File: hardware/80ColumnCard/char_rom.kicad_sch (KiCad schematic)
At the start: 3 parts, among them U20 2732, U20W28 '64 - '512, U20W32 '010 - '080

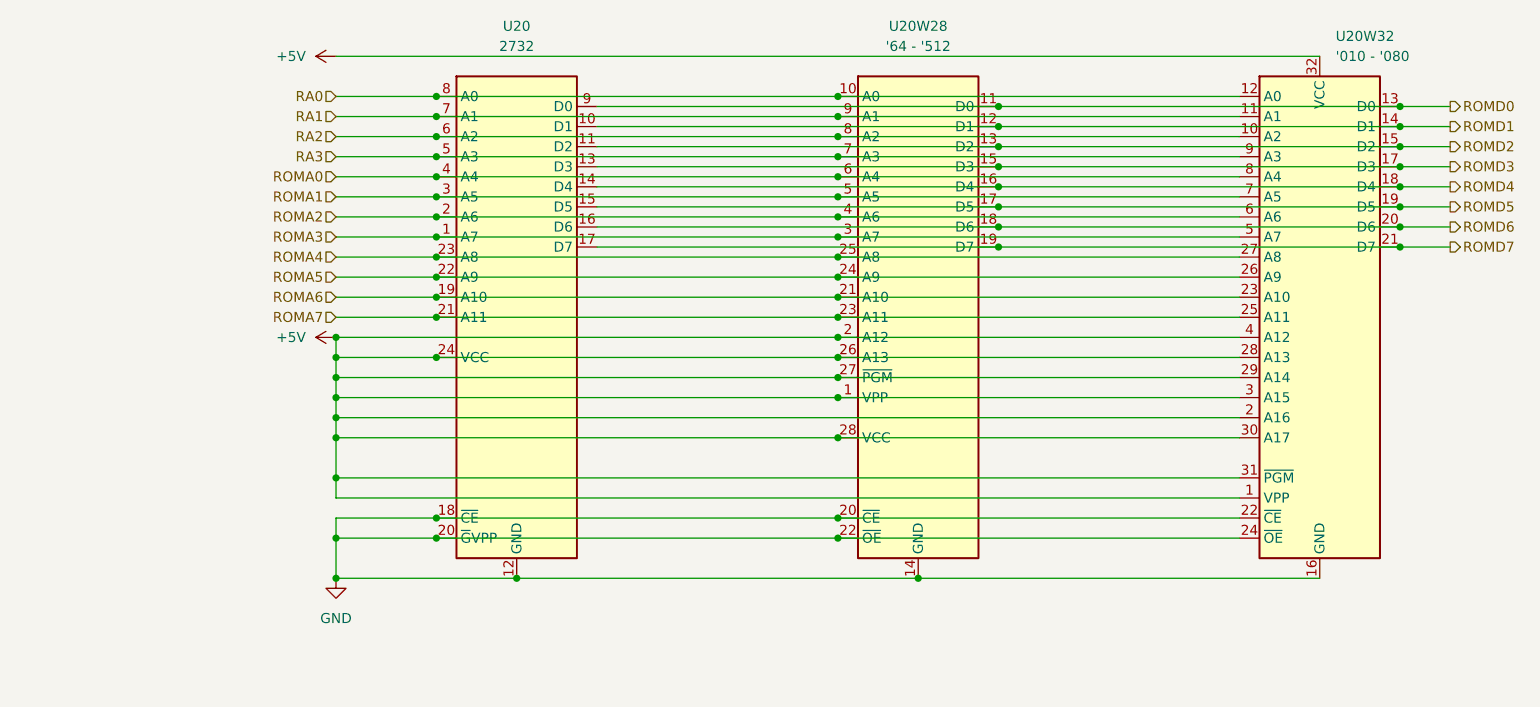
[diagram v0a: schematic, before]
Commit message: clean up, add jumpers for fw/char selection
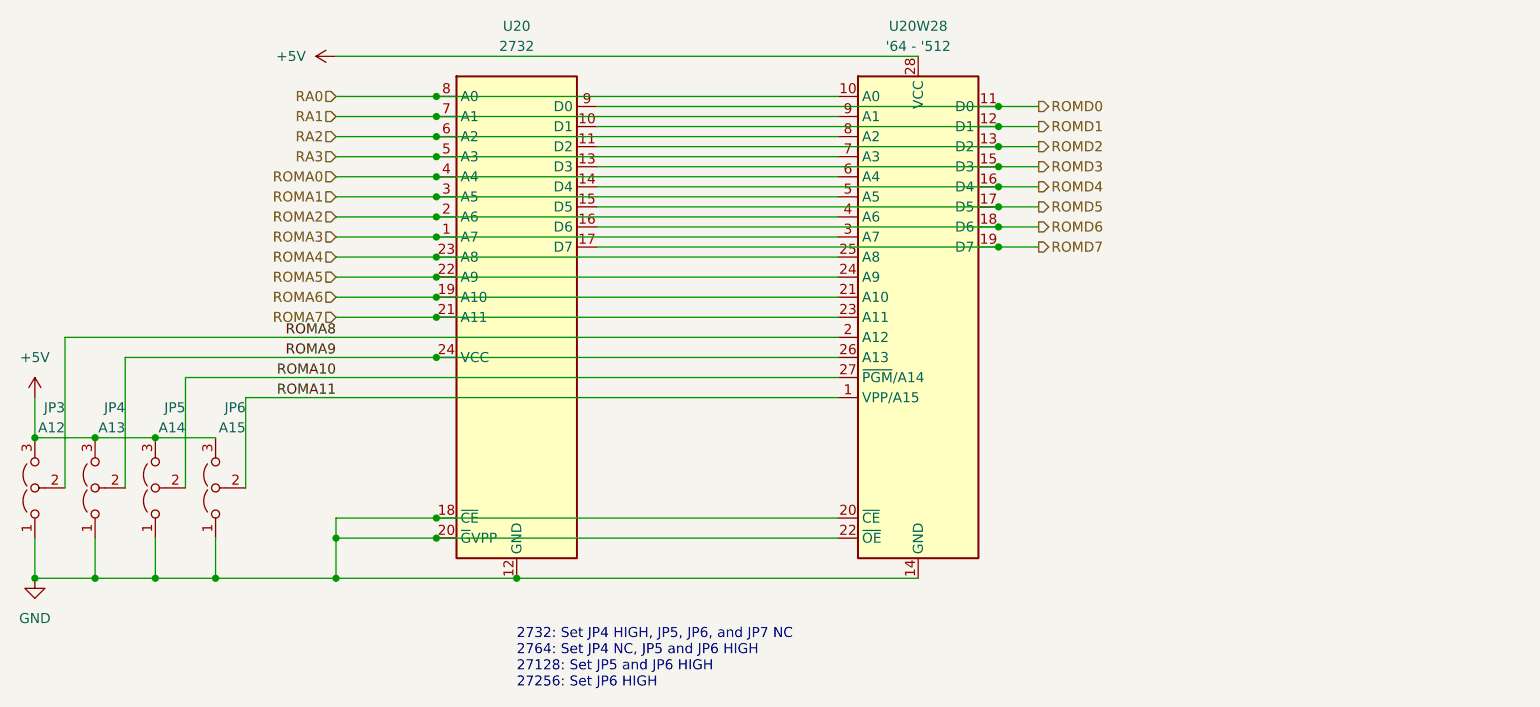
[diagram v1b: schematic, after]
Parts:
- removed U20W32: '010 - '080, Package_DIP:DIP-32_W15.24mm, symbol Memory_EPROM:27C020
- added JP3: A12, Connector_PinHeader_2.54mm:PinHeader_1x03_P2.54mm_Vertical, symbol Jumper:Jumper_3_Open
- added JP4: A13, Connector_PinHeader_2.54mm:PinHeader_1x03_P2.54mm_Vertical, symbol Jumper:Jumper_3_Open
- added JP5: A14, Connector_PinHeader_2.54mm:PinHeader_1x03_P2.54mm_Vertical, symbol Jumper:Jumper_3_Open
- added JP6: A15, Connector_PinHeader_2.54mm:PinHeader_1x03_P2.54mm_Vertical, symbol Jumper:Jumper_3_Open
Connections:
- net +5V: now also JP3.3 (B), JP4.3 (B), JP5.3 (B), JP6.3 (B); no longer U20.24 (VCC), U20W28.1 (VPP), U20W28.2 (A12), U20W28.26 (A13), U20W28.27 (~{PGM})
- net GND: now also JP3.1 (A), JP4.1 (A), JP5.1 (A), JP6.1 (A)
- new net ROMA10: JP5.2 (C), U20W28.27 (~{PGM}/A14)
- new net ROMA11: JP6.2 (C), U20W28.1 (VPP/A15)
- new net ROMA8: JP3.2 (C), U20W28.2 (A12)
- new net ROMA9: JP4.2 (C), U20.24 (VCC), U20W28.26 (A13)
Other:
- note added: "2732: Set JP4 HIGH, JP5, JP6, and JP7 NC 2764: Set JP4 NC, JP5 and JP6 HIGH 27128: Set JP5 and JP6 HIGH 27256: Set JP6 HIGH"
- moved on the sheet: U20W28

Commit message: revert fiddling
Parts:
- removed JP3: A12, Connector_PinHeader_2.54mm:PinHeader_1x03_P2.54mm_Vertical, symbol Jumper:Jumper_3_Open
- removed JP4: A13, Connector_PinHeader_2.54mm:PinHeader_1x03_P2.54mm_Vertical, symbol Jumper:Jumper_3_Open
- removed JP5: A14, Connector_PinHeader_2.54mm:PinHeader_1x03_P2.54mm_Vertical, symbol Jumper:Jumper_3_Open
- removed JP6: A15, Connector_PinHeader_2.54mm:PinHeader_1x03_P2.54mm_Vertical, symbol Jumper:Jumper_3_Open
- added U20C1: '010 - '080, Package_DIP:DIP-32_W15.24mm, symbol Memory_EPROM:27C020
- renumbered U20W28 to U20B1
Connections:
- net ROMA10 is gone; now on net +5V: U20B1.27 (~{PGM})
- net ROMA11 is gone; now on net +5V: U20B1.1 (VPP)
- net ROMA8 is gone; now on net +5V: U20B1.2 (A12)
- net ROMA9 is gone; now on net +5V: U20.24 (VCC), U20B1.26 (A13)
- net +5V: now also U20C1.1 (VPP), U20C1.2 (A16), U20C1.28 (A13), U20C1.29 (A14), U20C1.3 (A15), U20C1.30 (A17), U20C1.31 (~{PGM}), U20C1.32 (VCC), U20C1.4 (A12)
- net GND: now also U20C1.16 (GND), U20C1.22 (~{CE}), U20C1.24 (~{OE})
- net RA0: now also U20C1.12 (A0)
- net RA1: now also U20C1.11 (A1)
- net RA2: now also U20C1.10 (A2)
- net RA3: now also U20C1.9 (A3)
- net ROMA0: now also U20C1.8 (A4)
- net ROMA1: now also U20C1.7 (A5)
- net ROMA2: now also U20C1.6 (A6)
- net ROMA3: now also U20C1.5 (A7)
- net ROMA4: now also U20C1.27 (A8)
- net ROMA5: now also U20C1.26 (A9)
- net ROMA6: now also U20C1.23 (A10)
- net ROMA7: now also U20C1.25 (A11)
- net ROMD0: now also U20C1.13 (D0)
- net ROMD1: now also U20C1.14 (D1)
- net ROMD2: now also U20C1.15 (D2)
- net ROMD3: now also U20C1.17 (D3)
- net ROMD4: now also U20C1.18 (D4)
- net ROMD5: now also U20C1.19 (D5)
- net ROMD6: now also U20C1.20 (D6)
- net ROMD7: now also U20C1.21 (D7)
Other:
- note removed: "2732: Set JP4 HIGH, JP5, JP6, and JP7 NC 2764: Set JP4 NC, JP5 and JP6 HIGH 27128: Set JP5 and JP6 HIGH 27256: Set JP6 HIGH"
- moved on the sheet: U20B1

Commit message: Kicad 7, miscellaneous tweaks
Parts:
- removed U20C1: '010 - '080, Package_DIP:DIP-32_W15.24mm, symbol Memory_EPROM:27C020
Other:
- moved on the sheet: U20B1
